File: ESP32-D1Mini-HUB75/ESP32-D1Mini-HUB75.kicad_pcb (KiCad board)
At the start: 2 copper layers, 62 x 63.8 mm, 7 parts, among them J1 Conn_01x02, J2 Conn_01x02, J3 Conn_01x02, J4 Conn_02x08_Odd_Even, U1 mini_esp32

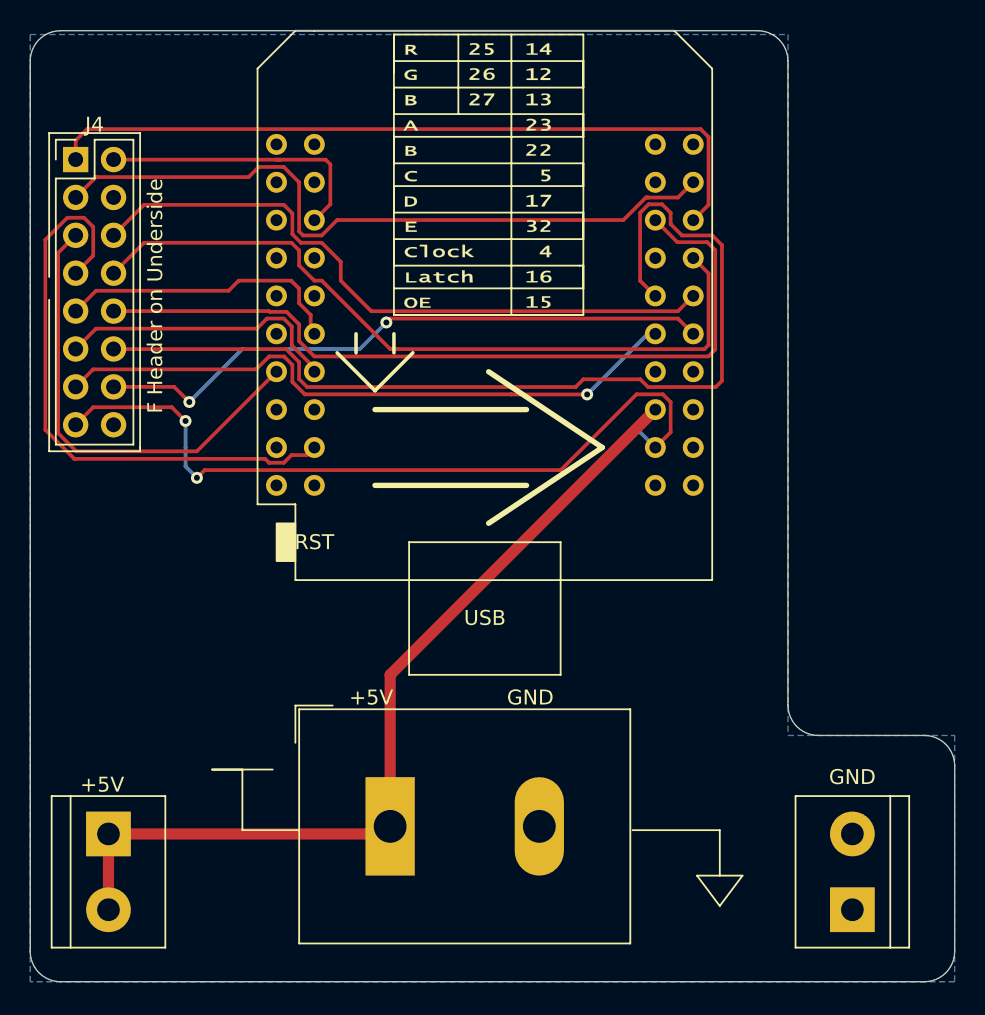
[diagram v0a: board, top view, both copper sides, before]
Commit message: updated screw terminal in esp32 hub75 board to use 8.5mm terminal that better suits the power cable that comes with the matrices
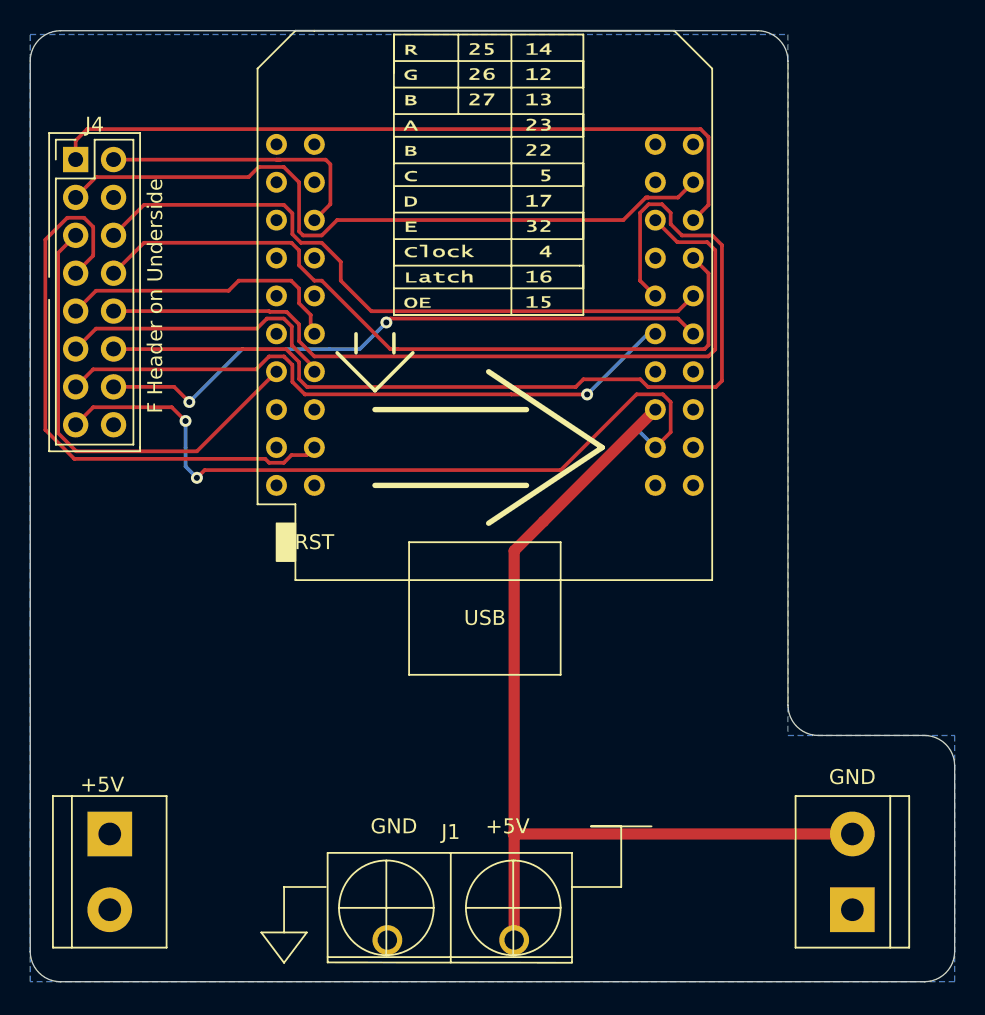
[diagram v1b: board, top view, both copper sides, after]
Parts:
- J1: footprint TerminalBlock_Dinkle:TerminalBlock_Dinkle_DT-55-B01X-02_P10.00mm -> ESP32-D1Mini-HUB75:KF8500-2P
- moved J2 50.1 mm to (126.0, 168.1), turned to 90 degrees
- moved J3 50.0 mm to (76.2, 163.1), turned to 270 degrees
- moved J1 8.64 mm to (99.1, 170.2), turned to 180 degrees
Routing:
- net +5V: track 59.5 -> 62.3 mm

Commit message: added plane to +5V for the power distribution between screw terminals
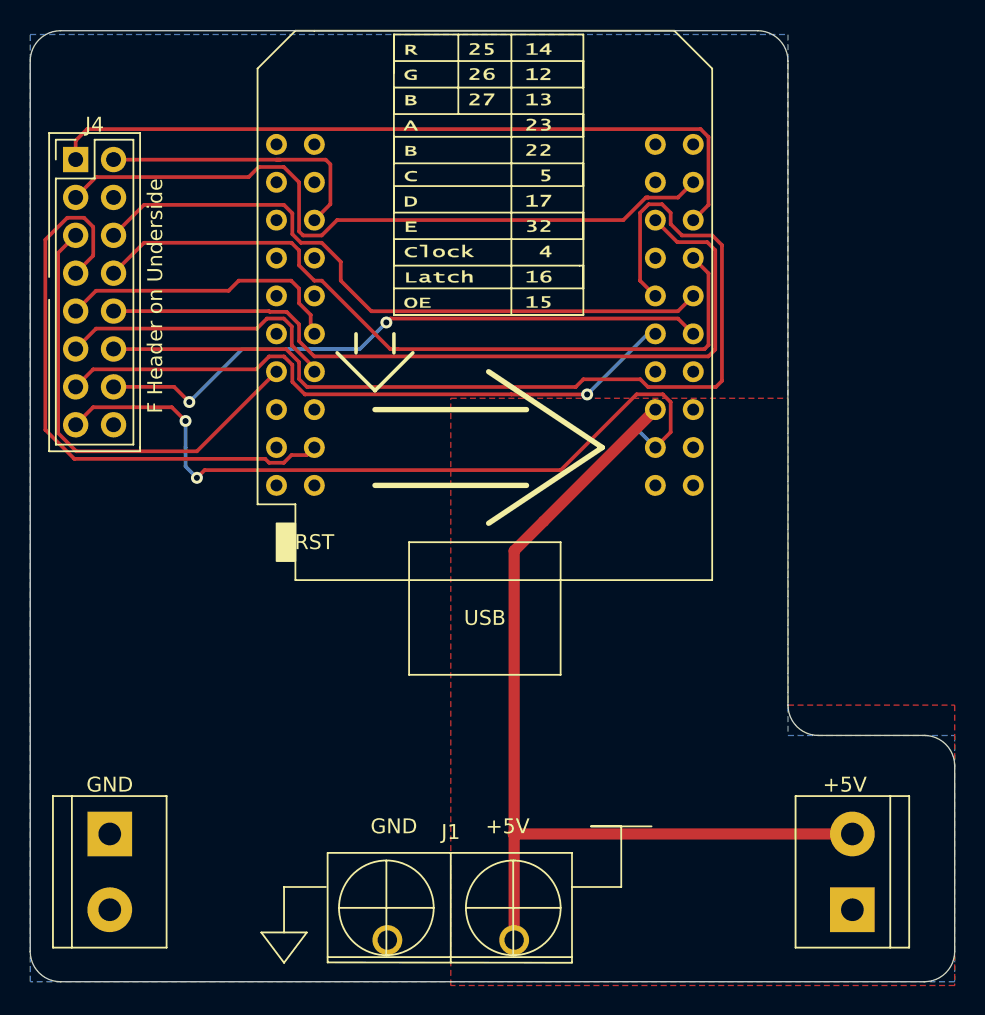
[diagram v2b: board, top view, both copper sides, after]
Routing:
- added copper zone on F.Cu, net +5V
